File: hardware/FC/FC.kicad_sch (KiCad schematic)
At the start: 33 parts, among them J1 USB-C, U1 STM32F722RET6, U2 TPS63070RNMR, U3 TL2575-33IKTTRG3, U4 ICM-20602, U5 BMP280

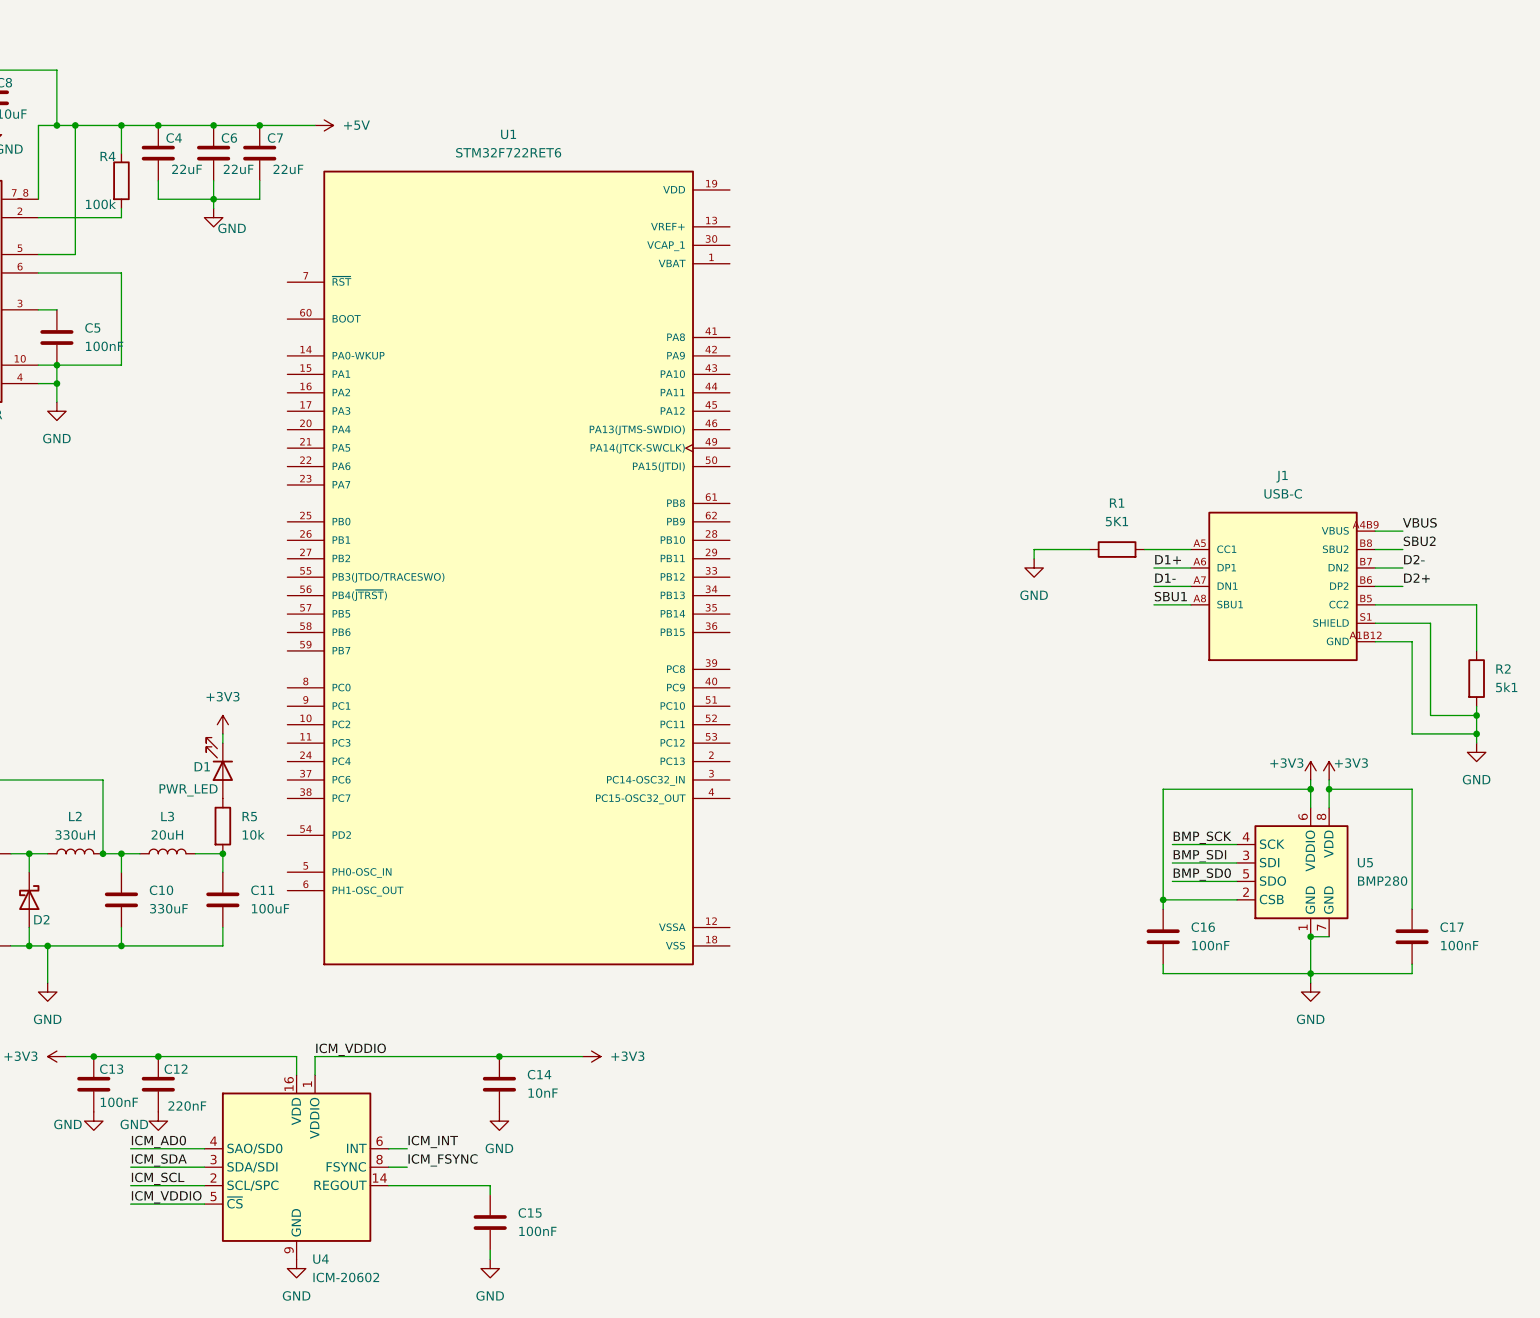
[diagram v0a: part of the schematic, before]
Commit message: added bmp580
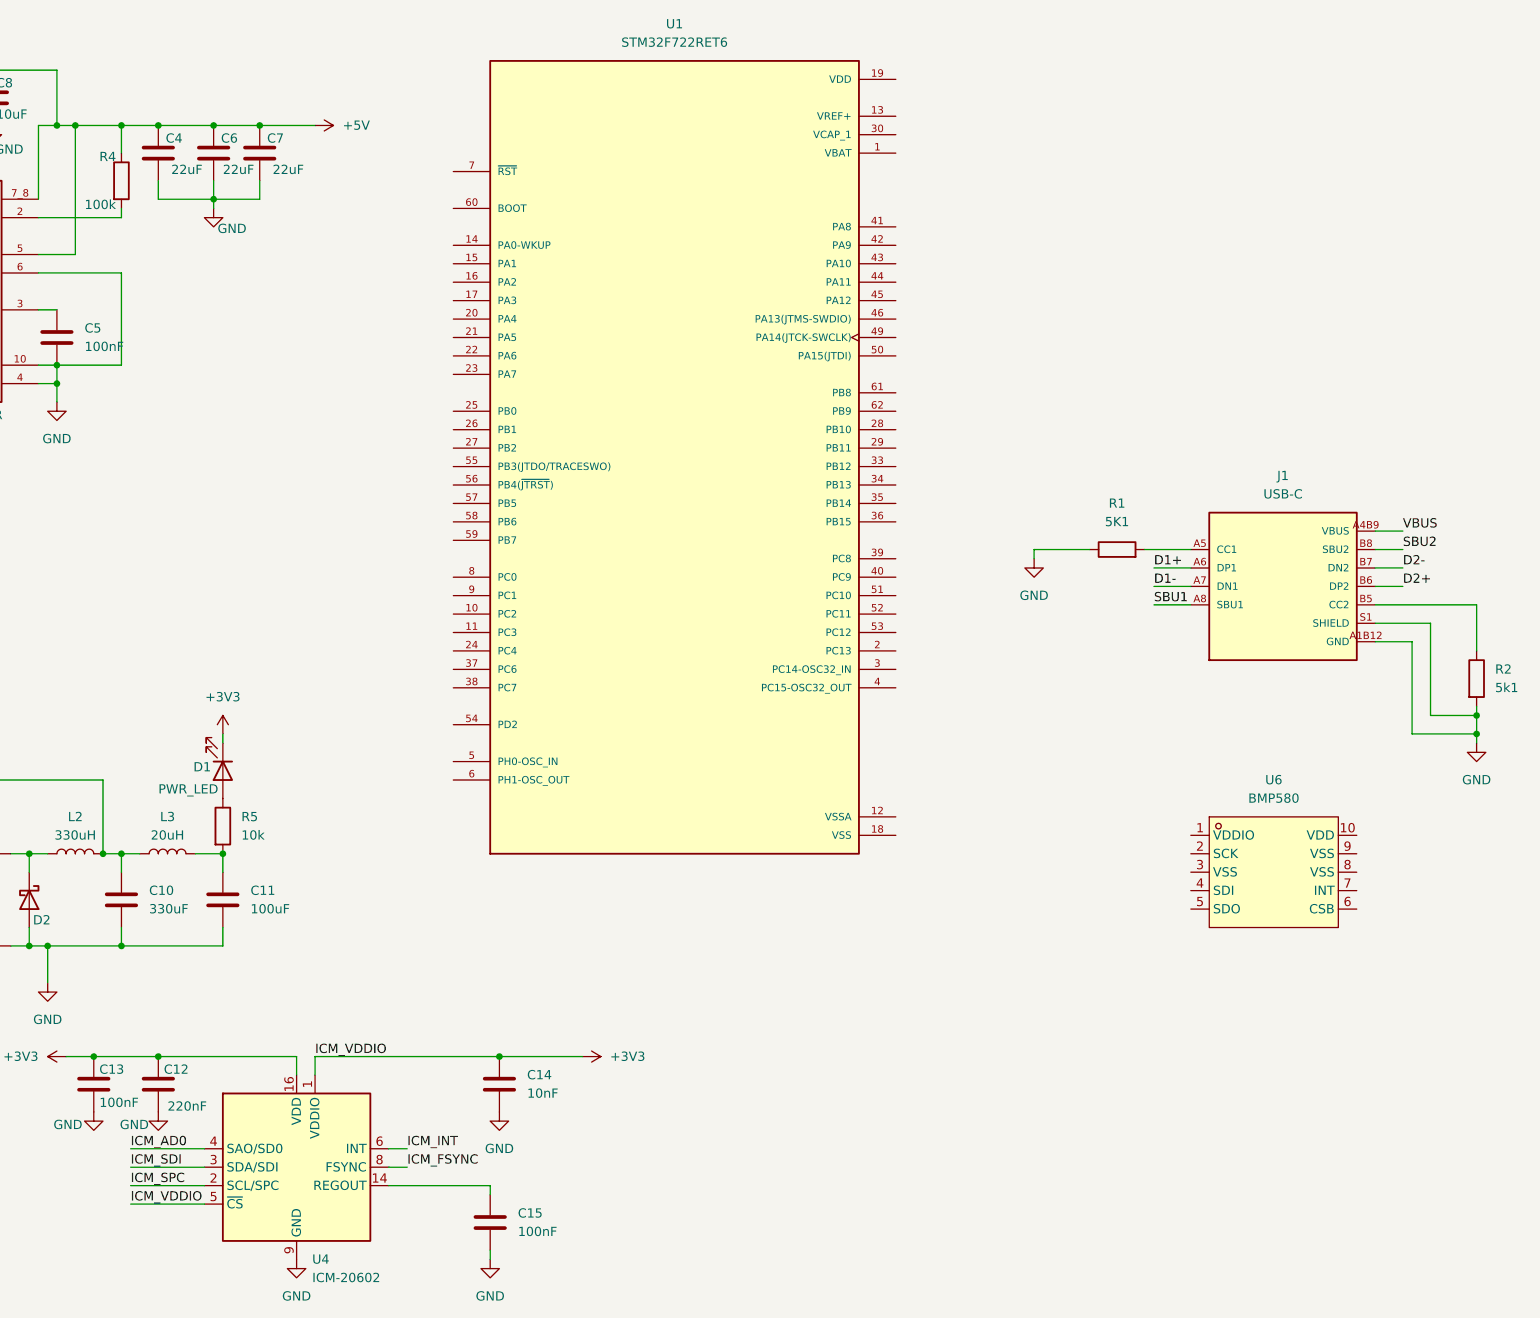
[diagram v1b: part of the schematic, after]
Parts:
- removed C16, C17: 100nF, symbol Device:C
- removed U5: BMP280, Package_LGA:Bosch_LGA-8_2x2.5mm_P0.65mm_ClockwisePinNumbering, symbol Sensor_Pressure:BMP280
- added U6: BMP580, FC_Sensors:LGA-10_L2.0-W2.0-P0.50-TL_BMP580, symbol FC_Sensord:BMP580
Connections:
- net ICM_SCL renamed ICM_SPC
- net ICM_SDA renamed ICM_SDI
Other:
- moved on the sheet: U1

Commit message: added lib files
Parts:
- removed C11: 100uF, symbol Device:C
- removed D1: PWR_LED, symbol Device:LED
- removed D2: D_Schottky, symbol Device:D_Schottky
- removed L2: 330uH, symbol Device:L
- removed L3: 20uH, symbol Device:L
- removed U3: TL2575-33IKTTRG3, TL2575-33IKTTRG3:VREG_TPS79625KTTR, symbol TL2575-33IKTTRG3:TL2575-33IKTTRG3
- added C16, C17, C18, C19, C20, C21, C22, C32: 100nF, symbol Device:C
- added C23: 2uF2, Capacitor_SMD:C_0805_2012Metric, symbol Device:C
- added C24, C25, C26, C27: 1uF, Capacitor_SMD:C_0805_2012Metric, symbol Device:C
- added C28, C29: 20pF, symbol Device:C
- added C30, C31: 2pF8, symbol Device:C
- added CN1: HC-0.8-8PWT, easyeda2kicad:CONN-SMD_8P-P0.80_HCTL_HC-0.8-8PWT, symbol CONN-SMD_8P-P0.80_HCTL_HC-0.8-8PWT:HC-0.8-8PWT
- added R6: 10K, symbol Device:R
- added R7: 470k, symbol Device:R
- added SW1, SW2: TS-1088-AR02016, RST_BTN:SW-SMD_L3.9-W3.0-P4.45, symbol SW-SMD_L3.9-W3.0-P4.45:TS-1088-AR02016
- added U5: AP2112K-3.3TRG1, easyeda2kicad:SOT-25-5_L2.9-W1.6-P0.95-LS2.8-BL, symbol AP2112K-3.3:AP2112K-3.3TRG1
- added X1: X322525MOB4SI, 25MHz_CRYSTAL:CRYSTAL-SMD_4P-L3.2-W2.5-BL, symbol CRYSTAL-SMD_4P-L3.2-W2.5-BL:X322525MOB4SI
- added X2: Q13FC1350000400, 32.768kHz_CRYSTAL:FC-135R_L3.2-W1.5, symbol FC-135R_L3.2-W1.5:Q13FC1350000400
- C1, C2, C3, C4, C6, C7, C8: footprint (none) -> Capacitor_SMD:C_0805_2012Metric
- C10: value 330uF -> 1uF; footprint (none) -> Capacitor_SMD:C_0805_2012Metric
- C9: value 100uF -> 1uF; footprint (none) -> Capacitor_SMD:C_0805_2012Metric
- R5: value 10k -> 150k
- U6: footprint FC_Sensors:LGA-10_L2.0-W2.0-P0.50-TL_BMP580 -> Package_LGA:Bosch_LGA-8_2x2.5mm_P0.65mm_ClockwisePinNumbering
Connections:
- net D1+ is gone; now on net USB_D1+: J1.A6 (DP1)
- net D1- is gone; now on net USB_D1-: J1.A7 (DN1)
- net ICM_AD0 is gone; now on net ICM_SD0: U4.4 (SAO/SD0)
- net ICM_FSYNC is gone; now on net GND: U4.8 (FSYNC)
- net ICM_SPC is gone; now on net ICM_SCK: U4.2 (SCL/SPC)
- net VDD is gone; now on net +3V3: U1.19 (VDD), U1.32 (VDD), U1.48 (VDD), U1.64 (VDD)
- net VSS is gone; now on net GND: U1.18 (VSS), U1.31 (VSS), U1.47 (VSS), U1.63 (VSS)
- net +3V3: now also C10.2, U1.1 (VBAT), U6.1 (VDDIO), U6.10 (VDD), C16.2, C17.2, C18.1, C19.1, C20.1, C21.1, C22.1, C24.1, C25.1, C26.1, C27.1, CN1.2, SW2.1, U5.5 (VOUT); no longer U4.5 (~{CS})
- net +5V: now also C9.2, R7.1, U5.1 (VIN), U5.3 (EN); no longer U2.5 (FB)
- net GND: now also C10.1, C9.1, R5.2, U1.12 (VSSA), U1.5 (PH0-OSC_IN), U1.6 (PH1-OSC_OUT), U6.3 (VSS), U6.5 (SDO), U6.6 (CSB), U6.8 (VSS), U6.9 (VSS), C16.1, C17.1, C18.2, C19.2, C20.2, C21.2, C22.2, C23.2, C24.2, C25.2, C26.2, C27.2, C28.1, C29.2, C30.2, C31.2, C32.1, CN1.1, CN1.10, CN1.9, R6.2, SW1.1, U5.2 (GND), X1.2 (GND), X1.4 (GND); no longer C10.2, C9.2
- net ICM_SDI: now also U1.23 (PA7)
- net VSYS: no longer C9.1
- net at R5.1: now also U2.5 (FB), R7.2
- net ESC_CURR: now reaches U1.14 (PA0-WKUP)
- net ESC_CURR: now also CN1.7
- net ICM_CS: now reaches U1.20 (PA4)
- net ICM_CS: now also U4.5 (~{CS})
- net ICM_SCK: now reaches U1.21 (PA5)
- net ICM_SD0: now reaches U1.22 (PA6)
- net LSE_IN: now reaches U1.3 (PC14-OSC32_IN)
- net LSE_IN: now also C30.1, X2.1
- net at U1.30 (VCAP_1): now also C23.1
- net ESC1: now reaches U1.37 (PC6)
- net ESC1: now also CN1.3
- net ESC2: now reaches U1.38 (PC7)
- net ESC2: now also CN1.4
- net ESC3: now reaches U1.39 (PC8)
- net ESC3: now also CN1.5
- net LSE_OUT: now reaches U1.4 (PC15-OSC32_OUT)
- net LSE_OUT: now also C31.1, X2.2
- net ESC4: now reaches U1.40 (PC9)
- net ESC4: now also CN1.6
- net USB_D1-: now reaches U1.44 (PA11)
- net USB_D1+: now reaches U1.45 (PA12)
- net ESC_TELE: now reaches U1.51 (PC10)
- net ESC_TELE: now also CN1.8
- net BMP_INT: now reaches U1.56 (PB4(~{JTRST}))
- net BMP_INT: now also U6.7 (INT)
- net I2C_SCL: now reaches U1.58 (PB6)
- net I2C_SCL: now also U6.2 (SCK)
- net I2C_SDA: now reaches U1.59 (PB7)
- net I2C_SDA: now also U6.4 (SDI)
- net BOOT: now reaches U1.60 (BOOT)
- net BOOT: now also R6.1, SW2.2
- net RESET: now reaches U1.7 (~{RST})
- net RESET: now also C32.2, SW1.2
- net D2+: no longer names the net of J1.B6 (DP2)
- net D2-: no longer names the net of J1.B7 (DN2)
- new net: C28.2, X1.1 (OSC1)
- new net: C29.1, X1.3 (OSC2)
- no-connect marks 0 -> 35
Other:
- moved on the sheet: R1

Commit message: sucsessful ERC, started PCB layout
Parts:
- added +V1, GND1: (no value), TestPoint:TestPoint_Pad_4.0x4.0mm, symbol Connector:TestPoint
- C12, C13, C15, C16, C17, C18, C19, C20, C21, C22, C32: footprint (none) -> Capacitor_SMD:C_0603_1608Metric
- C14, C28, C29, C30, C31: footprint (none) -> Capacitor_SMD:C_0402_1005Metric
- C4, C6, C7: footprint Capacitor_SMD:C_0805_2012Metric -> Capacitor_SMD:C_1206_3216Metric
- C5: footprint (none) -> Capacitor_SMD:C_0805_2012Metric
- CN1: footprint easyeda2kicad:CONN-SMD_8P-P0.80_HCTL_HC-0.8-8PWT -> CONNECTOR 8-PIN:CONN-SMD_8P-P0.80_HCTL_HC-0.8-8PWT
- L1: footprint (none) -> Inductor_SMD:L_0603_1608Metric
- R1, R2, R3, R4, R5, R6, R7: footprint (none) -> Resistor_SMD:R_0201_0603Metric
- U5: footprint easyeda2kicad:SOT-25-5_L2.9-W1.6-P0.95-LS2.8-BL -> AP2112K-3.3:AP2112K-3.3
- U6: footprint Package_LGA:Bosch_LGA-8_2x2.5mm_P0.65mm_ClockwisePinNumbering -> BMP580:LGA-10_L2.0-W2.0-P0.50-TL_BMP580
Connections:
- net +3V3: now also U1.13 (VREF+)
- net GND: now also GND1.1
- net VSYS: now also +V1.1
- no-connect marks 35 -> 34

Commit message: added pcb design
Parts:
- added H1, H2, H3, H4: MountingHole, MountingHole:MountingHole_2.2mm_M2, symbol Mechanical:MountingHole
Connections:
- net VBUS is gone; now on net +3V3: J1.A4B9 (VBUS), J1.B4A9 (VBUS)
- net ESC_TELE: now also U1.15 (PA1); no longer U1.51 (PC10)
- net GND: now also C29.1; no longer C29.2, U1.5 (PH0-OSC_IN), U1.6 (PH1-OSC_OUT)
- net ICM_CS: now also U1.21 (PA5); no longer U1.20 (PA4)
- net ICM_INT: now also U1.20 (PA4)
- net ICM_SCK: now also U1.24 (PC4); no longer U1.21 (PA5)
- net USB_D1+: now also U1.44 (PA11); no longer U1.45 (PA12)
- net USB_D1-: now also U1.45 (PA12); no longer U1.44 (PA11)
- net HSE_IN: now reaches C28.2, X1.1 (OSC1)
- net HSE_IN: now also U1.5 (PH0-OSC_IN)
- net HSE_OUT: now reaches X1.3 (OSC2)
- net HSE_OUT: now also C29.2, U1.6 (PH1-OSC_OUT); no longer C29.1
- net SBU1: no longer names the net of J1.A8 (SBU1)
- net SBU2: no longer names the net of J1.B8 (SBU2)
- no-connect marks 34 -> 35
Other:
- note added: "Barometer, IMU"
- note added: "Buttons"
- note added: "Connectors"
- note added: "Crystal Oscillators"
- note added: "Decoupling Capacitors"
- note added: "Low frequency, High frequency"
- note added: "Microcontroller"
- note added: "Mounting Holes"
- note added: "Power Supply"
- note added: "Pulse Converter, LDO"
- note added: "Reset, Boot"
- note added: "Sensors"
- note added: "USB-C, ESC connector"
- company: (none) -> Michal Olecki
- title: (none) -> Simple UAV Flight Controller
- moved on the sheet: +V1, C1, C10, C12, C13, C14, C15, C16, C17, C18, C19, C2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

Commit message: added LED for PS
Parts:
- added D1: LED, Diode_SMD:D_0805_2012Metric_Pad1.15x1.40mm_HandSolder, symbol Device:LED
- added J2: Conn_01x04_Pin, RADIO_SOLDER_PADS:radio_solder_pads, symbol Connector:Conn_01x04_Pin
- added R8: 150, symbol Device:R
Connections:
- net +3V3: now also R8.1
- net +5V: now also J2.2 (Pin_2)
- net GND: now also D1.1 (K), J2.1 (Pin_1)
- net RADIO_TX: now reaches U1.53 (PC12)
- net RADIO_TX: now also J2.4 (Pin_4)
- net RADIO_RX: now reaches U1.54 (PD2)
- net RADIO_RX: now also J2.3 (Pin_3)
- new net: D1.2 (A), R8.2
- no-connect marks 35 -> 33
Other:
- note added: "Radio Receiver Connector"
- moved on the sheet: C10

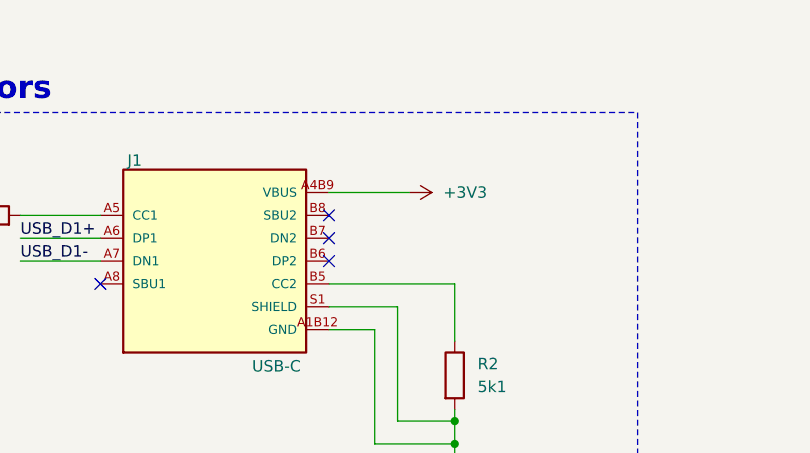
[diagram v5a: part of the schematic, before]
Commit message: fixed vbus line, added diode and graphic
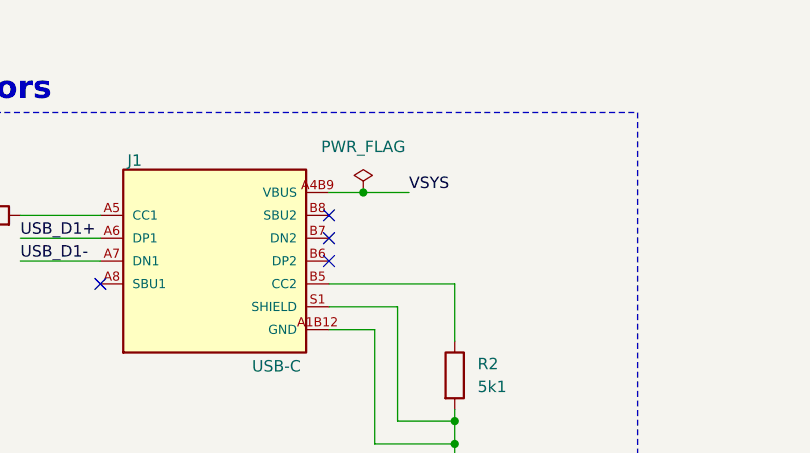
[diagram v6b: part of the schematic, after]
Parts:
- R8: footprint (none) -> Resistor_SMD:R_0603_1608Metric_Pad0.98x0.95mm_HandSolder
- U1: MANUFACTURER STMicroelectronics -> (none); Manufacturer (none) -> STMicroelectronics
- U2: MANUFACTURER Texas Instruments -> (none); Manufacturer (none) -> Texas Instruments
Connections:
- net +3V3: no longer J1.A4B9 (VBUS), J1.B4A9 (VBUS)
- net VSYS renamed VBUS
- net VBUS: now also J1.A4B9 (VBUS), J1.B4A9 (VBUS)
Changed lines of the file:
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@@
 	)
 	(junction
+		(at 345.44 39.37)
+		(diameter 0)
+		(color 0 0 0 0)
+	)
+	(junction
 		(at 97.79 205.74)
 		(diameter 0)
@@
 	(wire
 		(pts
-			(xy 341.63 39.37) (xy 350.52 39.37)
+			(xy 341.63 39.37) (xy 345.44 39.37)
 		)
 		(stroke
@@
 	(wire
 		(pts
+			(xy 345.44 39.37) (xy 350.52 39.37)
+		)
+		(stroke
+			(width 0)
+			(type default)
+		)
+	)
+	(wire
+		(pts
 			(xy 106.68 185.42) (xy 106.68 184.15)
 		)
@@
 		)
 	)
+	(label "VSYS"
+		(at 350.52 39.37 0)
+		(effects
+			(font
+				(size 1.27 1.27)
+			)
+			(justify left bottom)
+		)
+	)
 	(label "BMP_INT"
 		(at 170.18 165.1 0)
@@
 	)
 	(symbol
-		(lib_id "power:+3V3")
-		(at 350.52 39.37 270)
-		(unit 1)
-		(body_style 1)
-		(exclude_from_sim no)
-		(in_bom yes)
-		(on_board yes)
-		(in_pos_files yes)
-		(dnp no)
-		(fields_autoplaced yes)
-		(property "Reference" "#PWR047"
-			(at 346.71 39.37 0)
-			(hide yes)
-			(show_name no)
-			(do_not_autoplace no)
-			(effects
-				(font
-					(size 1.27 1.27)
-				)
-			)
-		)
-		(property "Value" "+3V3"
-			(at 354.33 39.3699 90)
-			(show_name no)
-			(do_not_autoplace no)
-			(effects
-				(font
-					(size 1.27 1.27)
-				)
-				(justify left)
-			)
-		)
-		(property "Footprint" ""
-			(at 350.52 39.37 0)
-			(hide yes)
-			(show_name no)
-			(do_not_autoplace no)
-			(effects
-				(font
-					(size 1.27 1.27)
-				)
-			)
-		)
-		(property "Datasheet" ""
-			(at 350.52 39.37 0)
-			(hide yes)
-			(show_name no)
-			(do_not_autoplace no)
-			(effects
-				(font
-					(size 1.27 1.27)
-				)
-			)
-		)
-		(property "Description" "Power symbol creates a global label with name \"+3V3\""
-			(at 350.52 39.37 0)
-			(hide yes)
-			(show_name no)
-			(do_not_autoplace no)
-			(effects
-				(font
-					(size 1.27 1.27)
-				)
-			)
-		)
-		(pin "1"
-		)
-		(instances
-			(project "FC"
-				(path "/392fbde6-20e0-4c59-b12e-738d483cde55"
-					(reference "#PWR047")
-					(unit 1)
-				)
-			)
-		)
-	)
-	(symbol
 		(lib_id "Device:C")
 		(at 227.33 64.77 0)
@@
 			)
 		)
-		(property "MANUFACTURER" "STMicroelectronics"
+		(property "Manufacturer" "STMicroelectronics"
 			(at 210.82 160.02 0)
 			(hide yes)
@@
 	)
 	(symbol
+		(lib_id "power:PWR_FLAG")
+		(at 345.44 39.37 0)
+		(unit 1)
+		(body_style 1)
+		(exclude_from_sim no)
+		(in_bom yes)
+		(on_board yes)
+		(in_pos_files yes)
+		(dnp no)
+		(fields_autoplaced yes)
+		(property "Reference" "#FLG02"
+			(at 345.44 37.465 0)
+			(hide yes)
+			(show_name no)
+			(do_not_autoplace no)
+			(effects
+				(font
+					(size 1.27 1.27)
+				)
+			)
+		)
+		(property "Value" "PWR_FLAG"
+			(at 345.44 34.29 0)
+			(show_name no)
+			(do_not_autoplace no)
+			(effects
+				(font
+					(size 1.27 1.27)
+				)
+			)
+		)
+		(property "Footprint" ""
+			(at 345.44 39.37 0)
+			(hide yes)
+			(show_name no)
+			(do_not_autoplace no)
+			(effects
+				(font
+					(size 1.27 1.27)
+				)
+			)
+		)
+		(property "Datasheet" ""
+			(at 345.44 39.37 0)
+			(hide yes)
+			(show_name no)
+			(do_not_autoplace no)
+			(effects
+				(font
+					(size 1.27 1.27)
+				)
+			)
+		)
+		(property "Description" "Special symbol for telling ERC where power comes from"
+			(at 345.44 39.37 0)
+			(hide yes)
+			(show_name no)
+			(do_not_autoplace no)
+			(effects
+				(font
+					(size 1.27 1.27)
+				)
+			)
+		)
+		(pin "1"
+		)
+		(instances
+			(project "FC"
+				(path "/392fbde6-20e0-4c59-b12e-738d483cde55"
+					(reference "#FLG02")
+					(unit 1)
+				)
+			)
+		)
+	)
+	(symbol
 		(lib_id "Device:C")
 		(at 356.87 152.4 0)
@@
 			)
 		)
-		(property "MANUFACTURER" "Texas Instruments"
+		(property "Manufacturer" "Texas Instruments"
 			(at 77.47 195.58 0)
 			(hide yes)
@@
 			)
 		)
-		(property "Footprint" ""
+		(property "Footprint" "Resistor_SMD:R_0603_1608Metric_Pad0.98x0.95mm_HandSolder"
 			(at 112.522 237.49 90)
 			(hide yes)
